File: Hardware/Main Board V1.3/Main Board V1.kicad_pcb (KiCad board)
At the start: 2 copper layers, 144.8 x 131.4 mm, 96 parts, among them J1 AUX GPIO, J10 Module 2, J11 VMot, J12 Module 3, J13 Shift Regs and Motor Drvs, J14 Module 4, J15 Module 5, J16 Micro_SD_Card, J17 Pin, J18 Pin, J19 Pin, J20 Pin, J21 Pin, J22 Pin, J23 RST, J24 RST, J3 Torch module, J4 Jumper, J5 Motor, J6 Module 1, J7 Ext Mot Drv, J8 01x02, J9 THC_Display, U1 ESP32_38p, U10 Y, U11 z, U12 A, U13 B, U14 C, U2 74LVC157A, U3 ESP32_38p, U4 BL8071CLATR33, U5 74AHCT595, U6 74AHCT595, U7 74AHCT595, U8 74AHCT595, U9 X

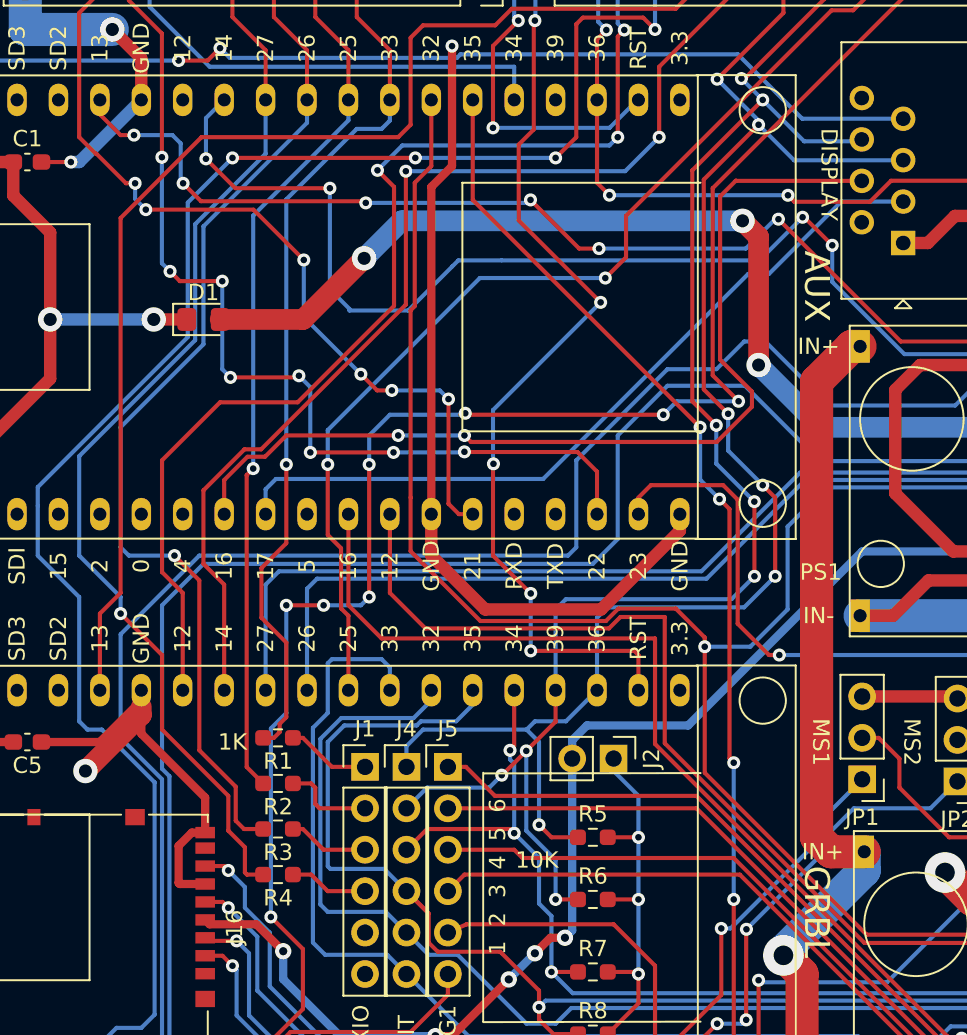
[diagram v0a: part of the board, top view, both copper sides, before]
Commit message: Pin Mapping update
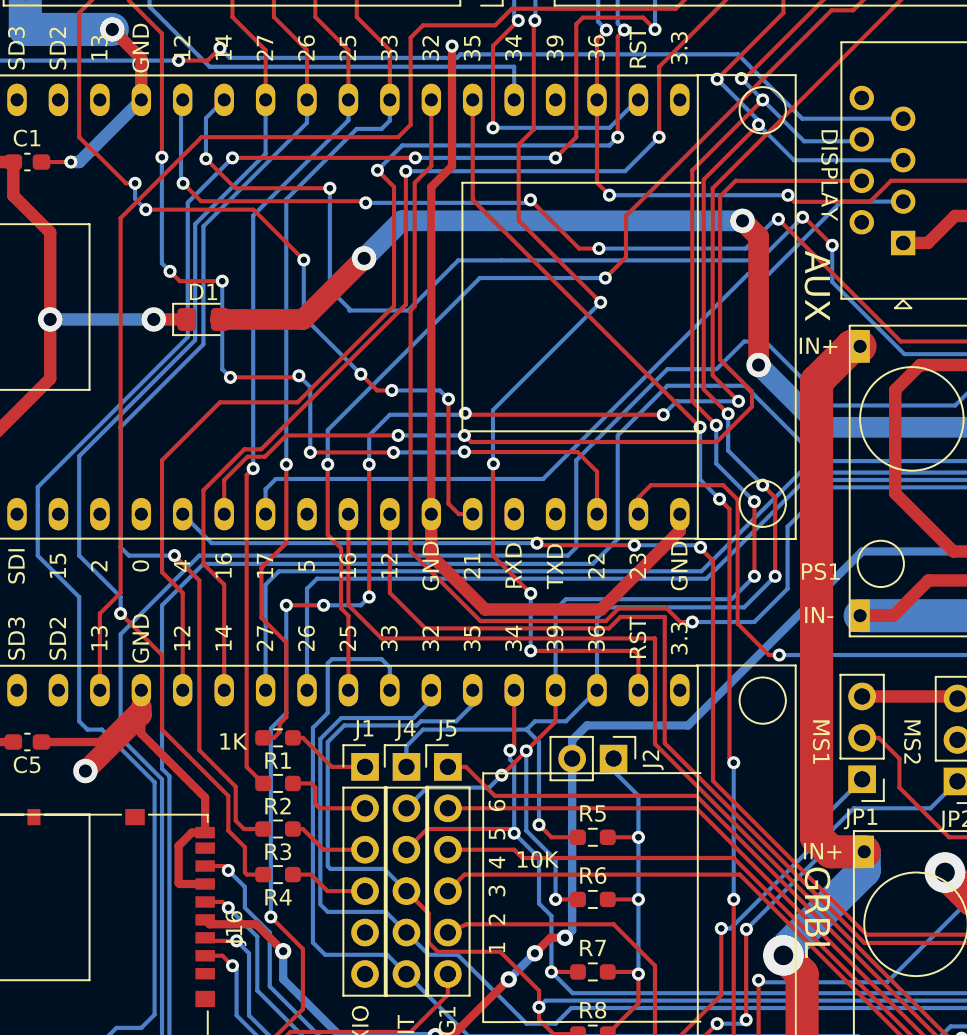
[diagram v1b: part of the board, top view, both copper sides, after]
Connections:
- U1 pad 32: unconnected-(U1-Pad32) -> Handover
- U1 pad 34: Handover -> unconnected-(U1-IO13-Pad34)
- U1 pad 7: unconnected-(U1-Pad7) -> MUX_SET
- U2 pad 1: TorchTrigger -> MUX_SET
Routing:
- net MUX_SET: track 0.00 -> 76.5 mm, vias 0 -> 3
- net TorchTrigger: track 171.8 -> 131.7 mm
- net Handover: track 104.7 -> 100.8 mm, vias 7 -> 6
